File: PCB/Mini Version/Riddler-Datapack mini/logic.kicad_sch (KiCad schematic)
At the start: 7 parts, among them SW1 RST, SW2 BOOT, U2 ESP32-S3-MINI-1

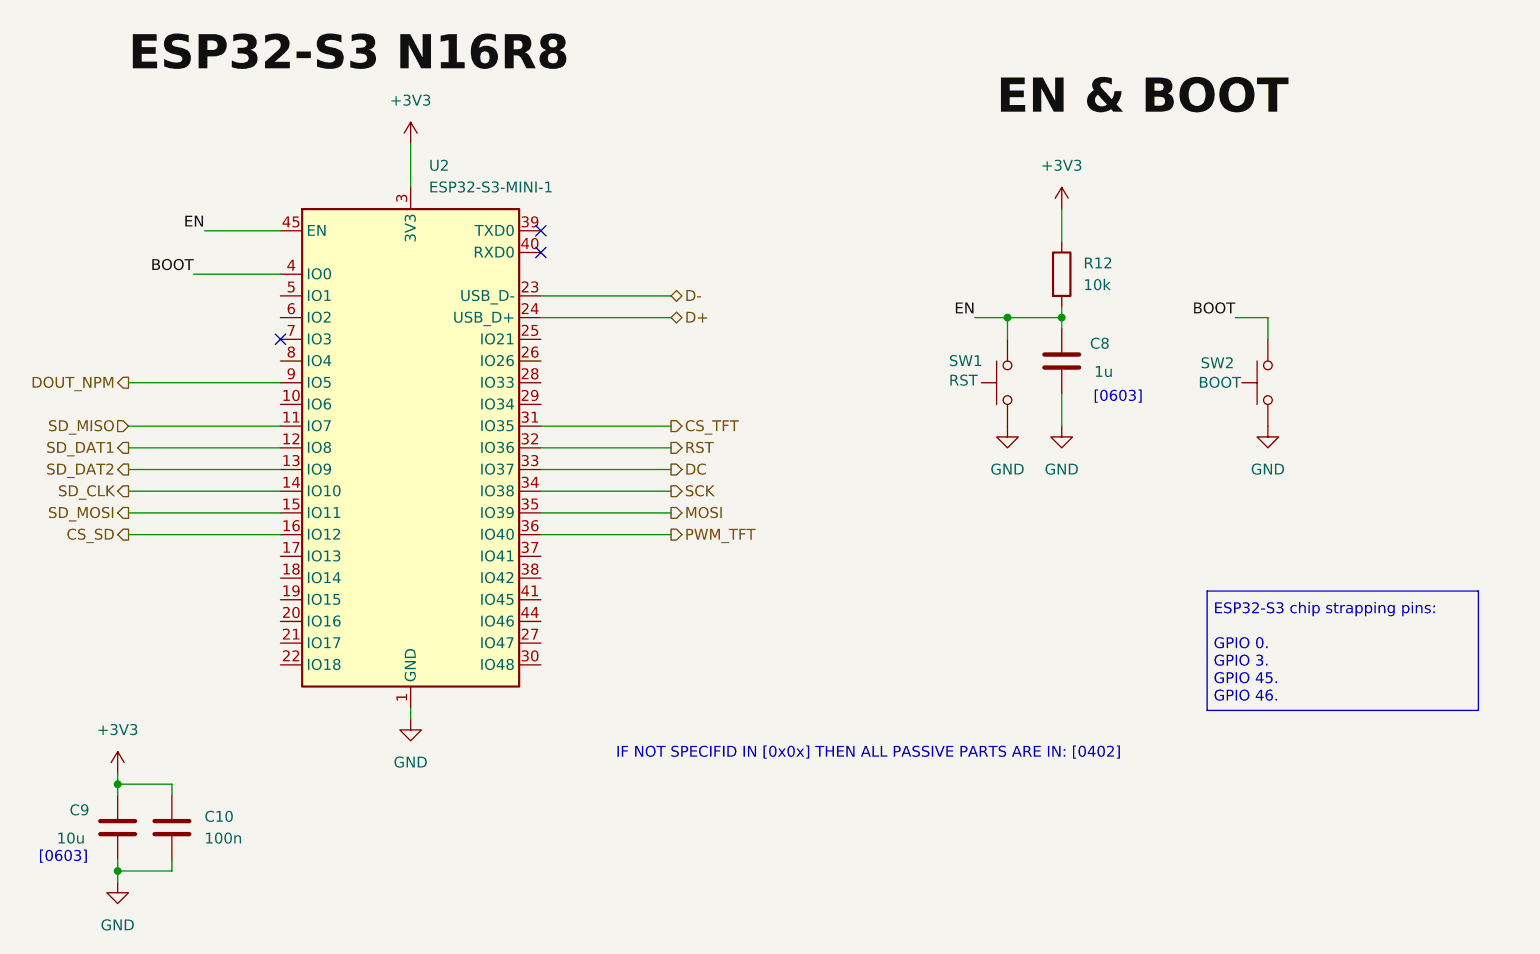
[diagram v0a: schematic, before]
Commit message: feat(hardware): complete 4-layer PCB routing for Mini Datapack prop and add 3D exports
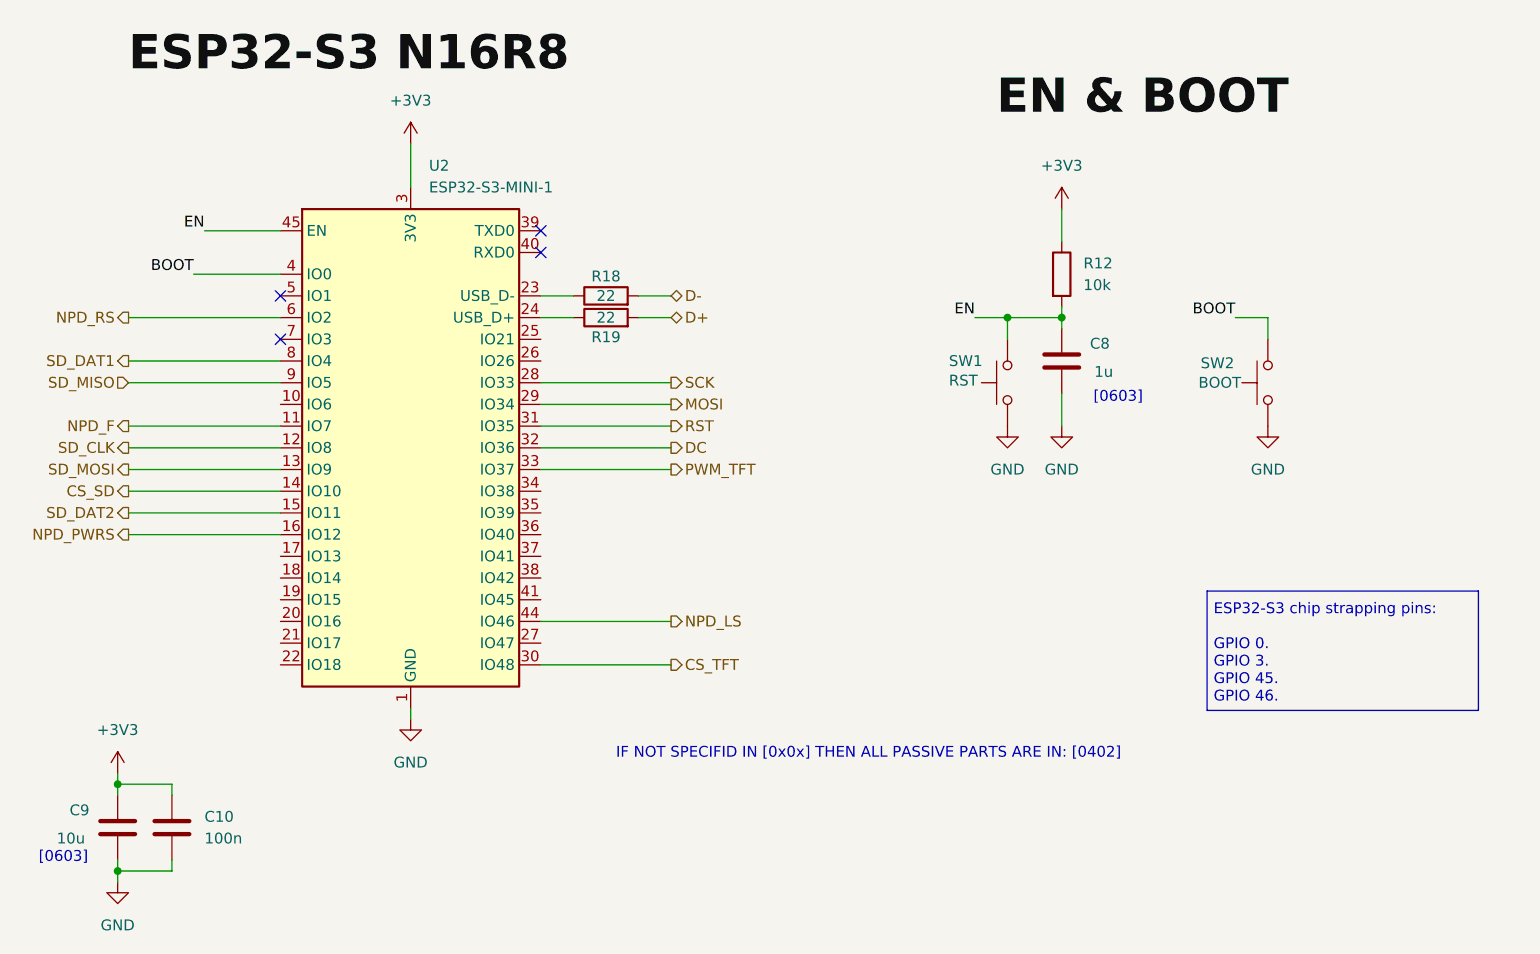
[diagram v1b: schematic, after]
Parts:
- added R18, R19: 22, Resistor_SMD:R_0402_1005Metric, symbol Device:R
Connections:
- net DOUT_NPM is gone; now on net SD_MISO: U2.9 (IO5)
- net CS_SD: now also U2.14 (IO10); no longer U2.16 (IO12)
- net CS_TFT: now also U2.30 (IO48); no longer U2.31 (IO35)
- net D+: now also R19.2; no longer U2.24 (USB_D+)
- net D-: now also R18.2; no longer U2.23 (USB_D-)
- net DC: now also U2.32 (IO36); no longer U2.33 (IO37)
- net MOSI: now also U2.29 (IO34); no longer U2.35 (IO39)
- net PWM_TFT: now also U2.33 (IO37); no longer U2.36 (IO40)
- net RST: now also U2.31 (IO35); no longer U2.32 (IO36)
- net SCK: now also U2.28 (IO33); no longer U2.34 (IO38)
- net SD_CLK: now also U2.12 (IO8); no longer U2.14 (IO10)
- net SD_DAT1: now also U2.8 (IO4); no longer U2.12 (IO8)
- net SD_DAT2: now also U2.15 (IO11); no longer U2.13 (IO9)
- net SD_MISO: no longer U2.11 (IO7)
- net SD_MOSI: now also U2.13 (IO9); no longer U2.15 (IO11)
- net NPD_LS: now reaches U2.44 (IO46)
- net NPD_RS: now reaches U2.6 (IO2)
- new net: R19.1, U2.24 (USB_D+)
- new net: R18.1, U2.23 (USB_D-)
- new net NPD_F: U2.11 (IO7)
- new net NPD_PWRS: U2.16 (IO12)
- no-connect marks 3 -> 4

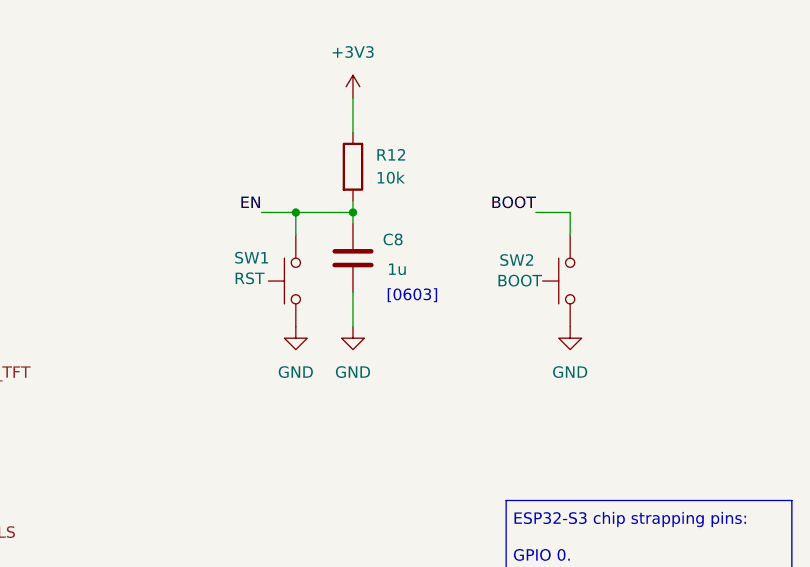
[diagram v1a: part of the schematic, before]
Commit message: Minor updates including: silkscreen design, and changed out the button
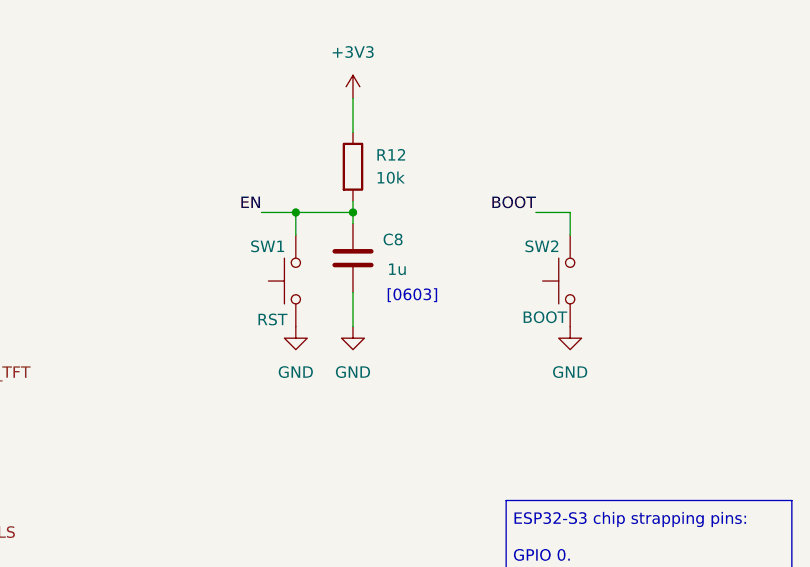
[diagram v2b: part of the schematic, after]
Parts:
- SW1, SW2: footprint Button_Switch_SMD:SW_Push_1P1T_NO_CK_KMR2 -> Button_Switch_SMD:SW_SPST_PTS810
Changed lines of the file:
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@@
-	)
-	(symbol
-		(lib_id "Switch:SW_Push")
-		(at 171.45 63.5 90)
-		(unit 1)
-		(body_style 1)
-		(exclude_from_sim no)
-		(in_bom yes)
-		(on_board yes)
-		(in_pos_files yes)
-		(dnp no)
-		(property "Reference" "SW2"
-			(at 163.576 61.214 90)
-			(show_name no)
-			(do_not_autoplace no)
-			(effects
-				(font
-					(size 1.27 1.27)
-				)
-				(justify right)
-			)
-		)
-		(property "Value" "BOOT"
-			(at 163.322 63.5 90)
-			(show_name no)
-			(do_not_autoplace no)
-			(effects
-				(font
-					(size 1.27 1.27)
-				)
-				(justify right)
-			)
-		)
-		(property "Footprint" "Button_Switch_SMD:SW_Push_1P1T_NO_CK_KMR2"
-			(at 166.37 63.5 0)
-			(hide yes)
-			(show_name no)
-			(do_not_autoplace no)
-			(effects
-				(font
-					(size 1.27 1.27)
-				)
-			)
-		)
-		(property "Datasheet" ""
-			(at 166.37 63.5 0)
-			(hide yes)
-			(show_name no)
-			(do_not_autoplace no)
-			(effects
-				(font
-					(size 1.27 1.27)
-				)
-			)
-		)
-		(property "Description" "Push button switch, generic, two pins"
-			(at 171.45 63.5 0)
-			(hide yes)
-			(show_name no)
-			(do_not_autoplace no)
-			(effects
-				(font
-					(size 1.27 1.27)
-				)
-			)
-		)
-		(pin "2"
-		)
-		(pin "1"
-		)
-		(instances
-			(project "Riddler-Datapack mini"
-				(path "/28edbdc5-6820-4039-a430-76d2ef240056/3a78c202-f18f-49be-8cf2-29b2d774bbf9"
-					(reference "SW2")
-					(unit 1)
-				)
-			)
-		)
 	)
 	(symbol
@@
 	)
 	(symbol
+		(lib_id "Switch:SW_Push")
+		(at 171.45 63.5 90)
+		(unit 1)
+		(body_style 1)
+		(exclude_from_sim no)
+		(in_bom yes)
+		(on_board yes)
+		(in_pos_files yes)
+		(dnp no)
+		(property "Reference" "SW2"
+			(at 166.37 59.69 90)
+			(show_name no)
+			(do_not_autoplace no)
+			(effects
+				(font
+					(size 1.27 1.27)
+				)
+				(justify right)
+			)
+		)
+		(property "Value" "BOOT"
+			(at 166.116 67.564 90)
+			(show_name no)
+			(do_not_autoplace no)
+			(effects
+				(font
+					(size 1.27 1.27)
+				)
+				(justify right)
+			)
+		)
+		(property "Footprint" "Button_Switch_SMD:SW_SPST_PTS810"
+			(at 166.37 63.5 0)
+			(hide yes)
+			(show_name no)
+			(do_not_autoplace no)
+			(effects
+				(font
+					(size 1.27 1.27)
+				)
+			)
+		)
+		(property "Datasheet" ""
+			(at 166.37 63.5 0)
+			(hide yes)
+			(show_name no)
+			(do_not_autoplace no)
+			(effects
+				(font
+					(size 1.27 1.27)
+				)
+			)
+		)
+		(property "Description" "Push button switch, generic, two pins"
+			(at 171.45 63.5 0)
+			(hide yes)
+			(show_name no)
+			(do_not_autoplace no)
+			(effects
+				(font
+					(size 1.27 1.27)
+				)
+			)
+		)
+		(pin "2"
+		)
+		(pin "1"
+		)
+		(instances
+			(project "Riddler-Datapack mini"
+				(path "/28edbdc5-6820-4039-a430-76d2ef240056/3a78c202-f18f-49be-8cf2-29b2d774bbf9"
+					(reference "SW2")
+					(unit 1)
+				)
+			)
+		)
+	)
+	(symbol
+		(lib_id "Switch:SW_Push")
+		(at 140.97 63.5 90)
+		(unit 1)
+		(body_style 1)
+		(exclude_from_sim no)
+		(in_bom yes)
+		(on_board yes)
+		(in_pos_files yes)
+		(dnp no)
+		(property "Reference" "SW1"
+			(at 135.89 59.69 90)
+			(show_name no)
+			(do_not_autoplace no)
+			(effects
+				(font
+					(size 1.27 1.27)
+				)
+				(justify right)
+			)
+		)
+		(property "Value" "RST"
+			(at 136.652 67.818 90)
+			(show_name no)
+			(do_not_autoplace no)
+			(effects
+				(font
+					(size 1.27 1.27)
+				)
+				(justify right)
+			)
+		)
+		(property "Footprint" "Button_Switch_SMD:SW_SPST_PTS810"
+			(at 135.89 63.5 0)
+			(hide yes)
+			(show_name no)
+			(do_not_autoplace no)
+			(effects
+				(font
+					(size 1.27 1.27)
+				)
+			)
+		)
+		(property "Datasheet" ""
+			(at 135.89 63.5 0)
+			(hide yes)
+			(show_name no)
+			(do_not_autoplace no)
+			(effects
+				(font
+					(size 1.27 1.27)
+				)
+			)
+		)
+		(property "Description" "Push button switch, generic, two pins"
+			(at 140.97 63.5 0)
+			(hide yes)
+			(show_name no)
+			(do_not_autoplace no)
+			(effects
+				(font
+					(size 1.27 1.27)
+				)
+			)
+		)
+		(pin "2"
+		)
+		(pin "1"
+		)
+		(instances
+			(project "Riddler-Datapack mini"
+				(path "/28edbdc5-6820-4039-a430-76d2ef240056/3a78c202-f18f-49be-8cf2-29b2d774bbf9"
+					(reference "SW1")
+					(unit 1)
+				)
+			)
+		)
+	)
+	(symbol
 		(lib_id "power:GND")
 		(at 147.32 68.58 0)
@@
 					(unit 1)
 				)
-			)
-		)
-	)
-	(symbol
-		(lib_id "Switch:SW_Push")
-		(at 140.97 63.5 90)
-		(unit 1)
-		(body_style 1)
-		(exclude_from_sim no)
-		(in_bom yes)
-		(on_board yes)
-		(in_pos_files yes)
-		(dnp no)
-		(property "Reference" "SW1"
-			(at 134.112 60.96 90)
-			(show_name no)
-			(do_not_autoplace no)
-			(effects
-				(font
-					(size 1.27 1.27)
-				)
-				(justify right)
-			)
-		)
-		(property "Value" "RST"
-			(at 134.112 63.246 90)
-			(show_name no)
-			(do_not_autoplace no)
-			(effects
-				(font
-					(size 1.27 1.27)
-				)
-				(justify right)
-			)
-		)
-		(property "Footprint" "Button_Switch_SMD:SW_Push_1P1T_NO_CK_KMR2"
-			(at 135.89 63.5 0)
-			(hide yes)
-			(show_name no)
-			(do_not_autoplace no)
-			(effects
-				(font
-					(size 1.27 1.27)
-				)
-			)
-		)
-		(property "Datasheet" ""
-			(at 135.89 63.5 0)
-			(hide yes)
-			(show_name no)
-			(do_not_autoplace no)
-			(effects
-				(font
-					(size 1.27 1.27)
-				)
-			)
-		)
-		(property "Description" "Push button switch, generic, two pins"
-			(at 140.97 63.5 0)
-			(hide yes)
-			(show_name no)
-			(do_not_autoplace no)
-			(effects
-				(font
-					(size 1.27 1.27)
-				)
-			)
-		)
-		(pin "2"
-		)
-		(pin "1"
-		)
-		(instances
-			(project "Riddler-Datapack mini"
-				(path "/28edbdc5-6820-4039-a430-76d2ef240056/3a78c202-f18f-49be-8cf2-29b2d774bbf9"
-					(reference "SW1")
-					(unit 1)
-				)

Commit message: v1.1: update Mini Datapack with repositioned USB-C, relief vias, and v1p1 exports
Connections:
- net MISO: now reaches U2.26 (IO26)
- net CS_SD2: now reaches U2.27 (IO47)
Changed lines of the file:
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@@
+	(wire
+		(pts
+			(xy 86.36 60.96) (xy 101.6 60.96)
+		)
+		(stroke
+			(width 0)
+			(type default)
+		)
+	)
 	(wire
 		(pts
@@
 		(pts
 			(xy 147.32 43.18) (xy 147.32 46.99)
+		)
+		(stroke
+			(width 0)
+			(type default)
+		)
+	)
+	(wire
+		(pts
+			(xy 86.36 93.98) (xy 101.6 93.98)
 		)
 		(stroke
@@
 		)
 	)
+	(hierarchical_label "MISO"
+		(shape input)
+		(at 101.6 60.96 0)
+		(effects
+			(font
+				(size 1.27 1.27)
+			)
+			(justify left)
+		)
+	)
 	(hierarchical_label "MOSI"
 		(shape output)
@@
 		)
 	)
+	(hierarchical_label "CS_SD2"
+		(shape output)
+		(at 101.6 93.98 0)
+		(effects
+			(font
+				(size 1.27 1.27)
+			)
+			(justify left)
+		)
+	)
